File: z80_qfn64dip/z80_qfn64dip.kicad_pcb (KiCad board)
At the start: 4 copper layers, 60 x 23 mm, 48 parts, among them J1 Conn_08, U1 Caravel_QFN, U2 Z80CPU, U3 TPS7A2018PDQNRM3, U4 TPS7A2033PDQNRM3, U5 TPS7A2050PDQNRM3, U6 AT25EU0081A

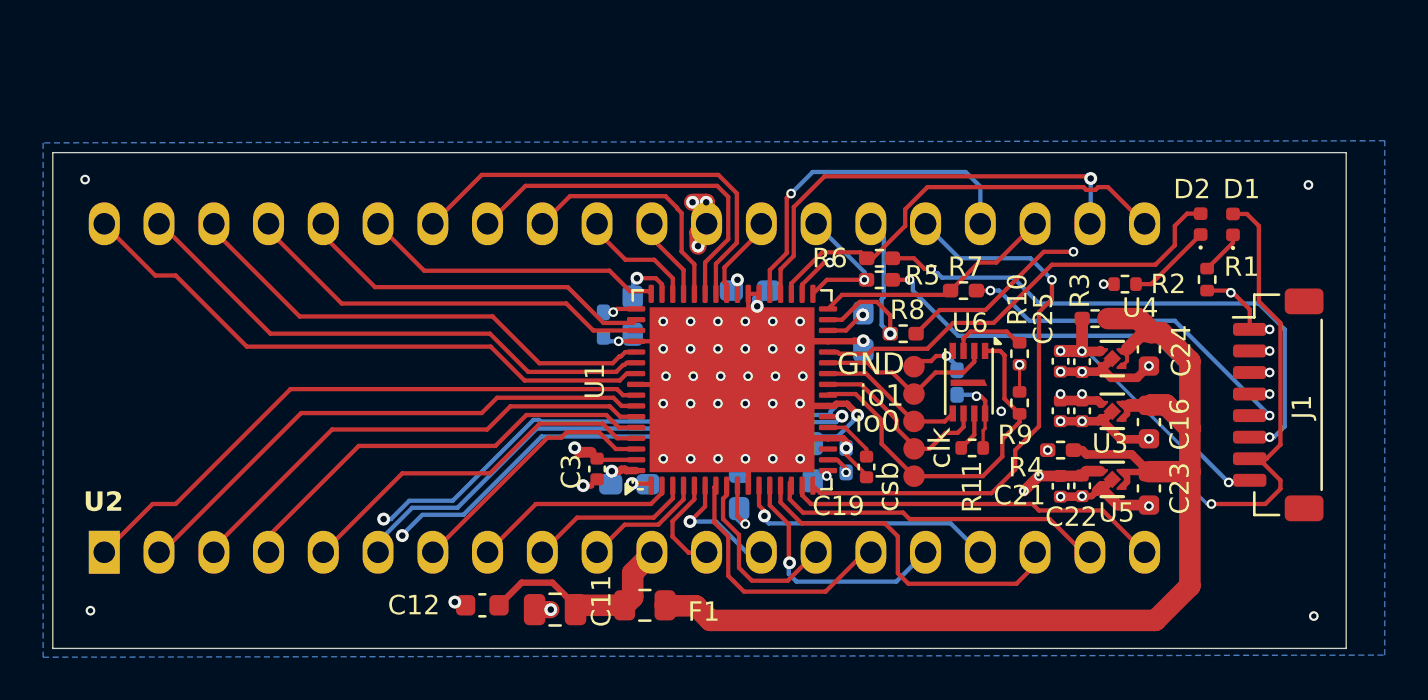
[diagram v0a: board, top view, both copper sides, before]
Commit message: minor layout position tweaks; move schematics around a bit; add aisler user design rule
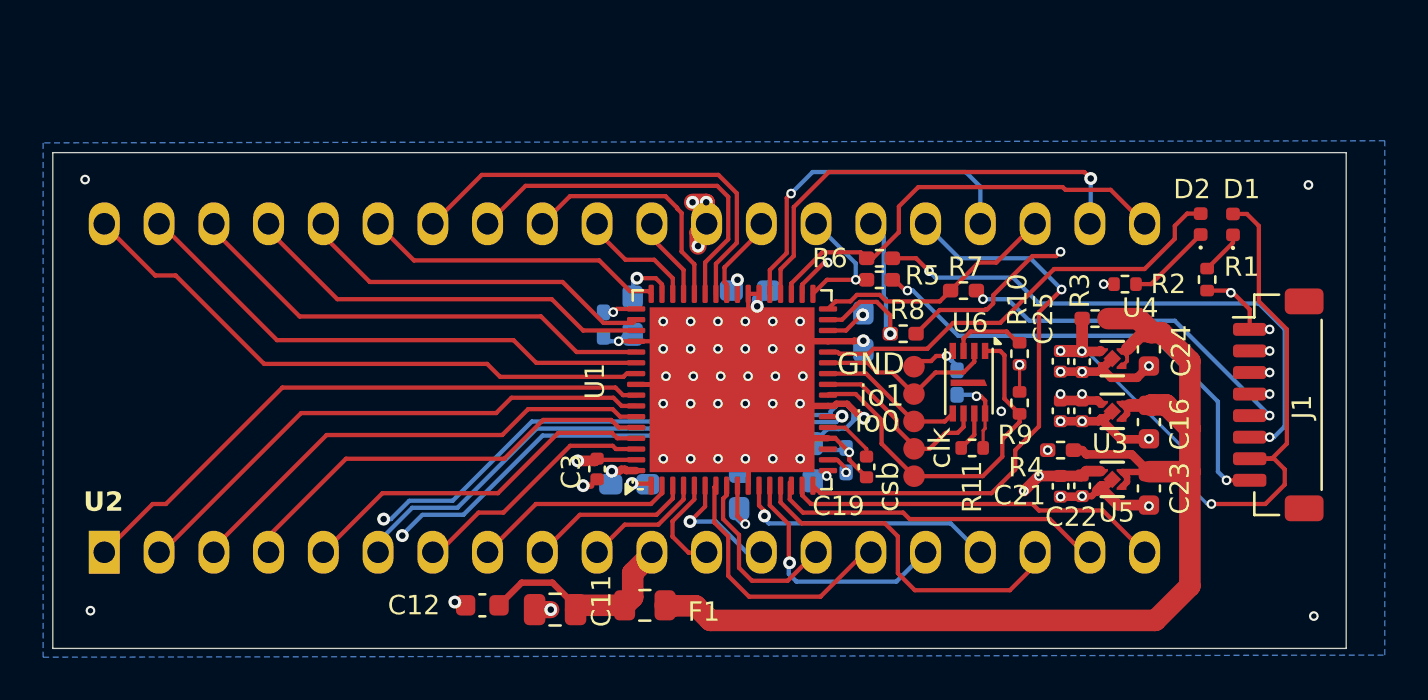
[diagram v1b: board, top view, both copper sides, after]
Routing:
- net GND: track 118.6 -> 121.8 mm
- net HK_CSB: track 26.3 -> 25.2 mm
- net VDDA: track 77.9 -> 78.8 mm
- net /prj_io24: track 12.1 -> 11.6 mm

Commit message: remove signals from power layer moving them to bottom layer; change power routing from tracks to planes if they can be called as such
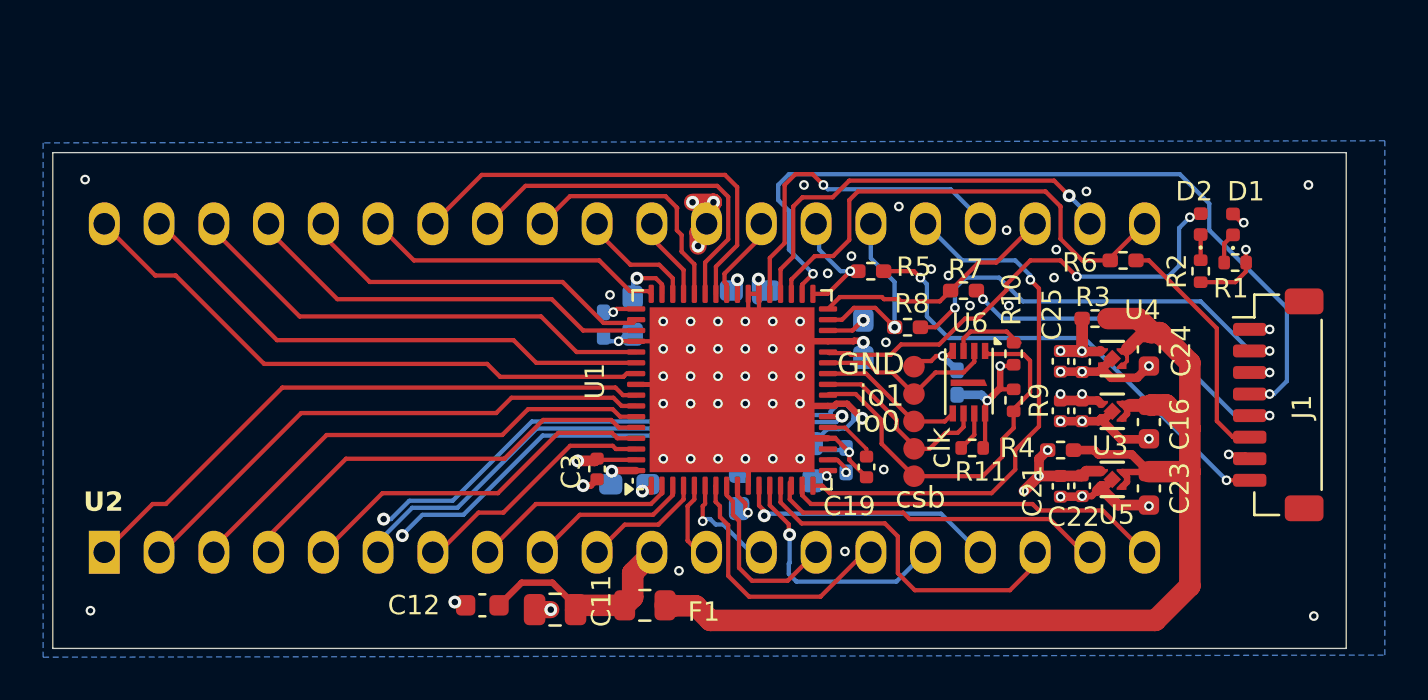
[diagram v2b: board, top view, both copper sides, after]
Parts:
- moved R6 11.3 mm to (166.2, 77.5)
- moved R2 3.56 mm to (169.7, 78.0), turned to -90 degrees
- moved R1 1.52 mm to (171.3, 77.6), turned to 0 degrees
- moved R5 0.57 mm to (154.4, 78.0)
- moved R8 0.36 mm to (156.2, 80.6)
- moved C6 0.34 mm to (154.1, 81.1)
- moved R9 0.30 mm to (161.1, 84.0)
- moved R10 0.28 mm to (161.1, 81.8)
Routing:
- net Net-(J1-Pin_6): track 25.9 -> 11.2 mm, vias 2 -> 0
- net VDDA: track 78.8 -> 66.0 mm, vias 9 -> 10
- net HK_CSB: track 25.2 -> 37.5 mm
- net Net-(D2-K): track 3.95 -> 1.19 mm
- net HK_SCK: track 20.4 -> 22.7 mm
- net VDDIO: track 31.1 -> 29.0 mm
- net /prj_io37: track 26.8 -> 25.5 mm
- net ser_rx: track 21.0 -> 19.6 mm
- net Net-(J1-Pin_2): track 20.1 -> 19.1 mm
- net GND: track 121.8 -> 122.7 mm, vias 63 -> 78
- net flash_csb: track 17.0 -> 18.0 mm
- net gpio: track 20.4 -> 21.3 mm, vias 0 -> 2
- net /prj_io28: track 4.65 -> 3.77 mm
- net HK_JTAG: track 9.82 -> 8.95 mm
- net HK_SDI: track 6.12 -> 5.29 mm
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- added copper zone on In2.Cu, net VCCD
- added copper zone on In2.Cu, net VDDIO

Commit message: minor changes
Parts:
- U3: value TPS7A2018PDQNRM3 -> TPS7A2033PDQNRM3
- U4: value TPS7A2033PDQNRM3 -> TPS7A2018PDQNRM3
- moved U4 2.48 mm to (165.7, 84.5)
- moved U3 2.45 mm to (165.7, 82.1)
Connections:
- U3 pad 1: VCCD -> VDDA
- U4 pad 1: VDDA -> VCCD
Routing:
- net /prj_io10: track 11.4 -> 9.42 mm, vias 0 -> 1
- net GND: vias 78 -> 101
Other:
- board text added: "Z80 V1"

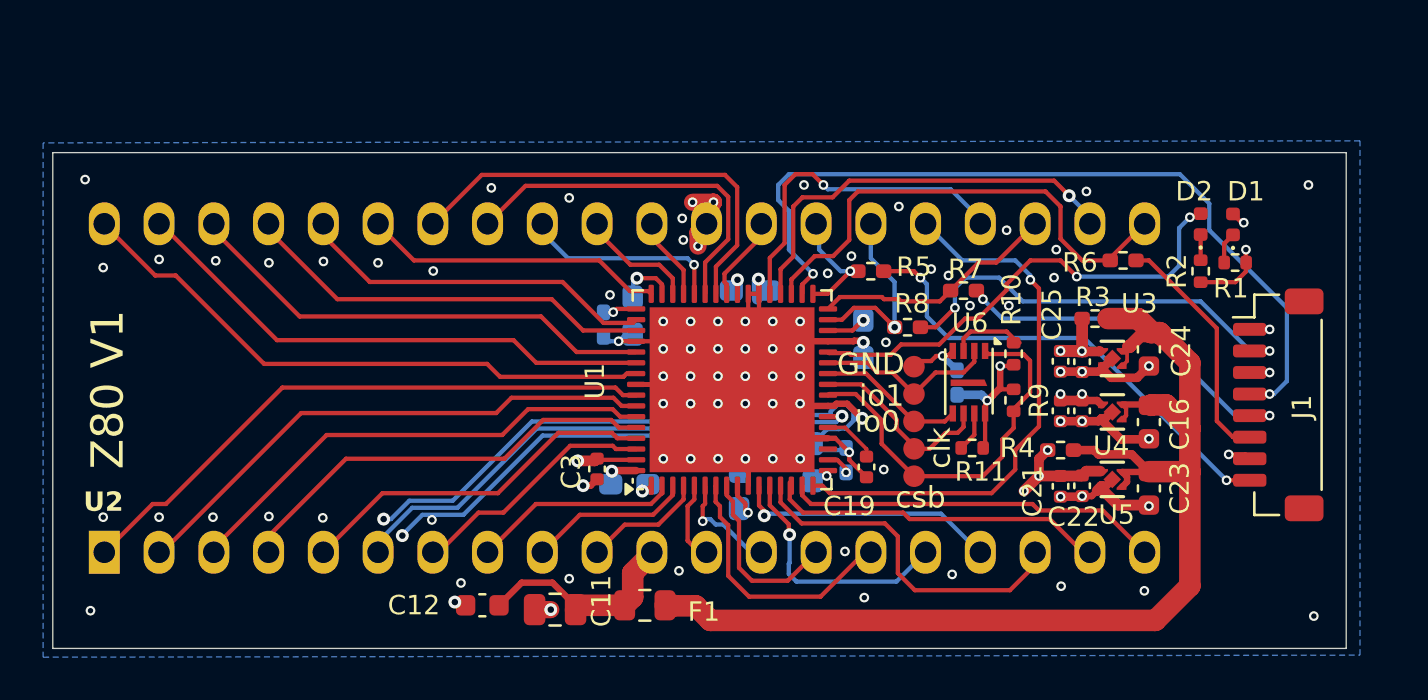
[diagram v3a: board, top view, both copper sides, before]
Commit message: mainly layout changes, remove kicad_prl from comitted files
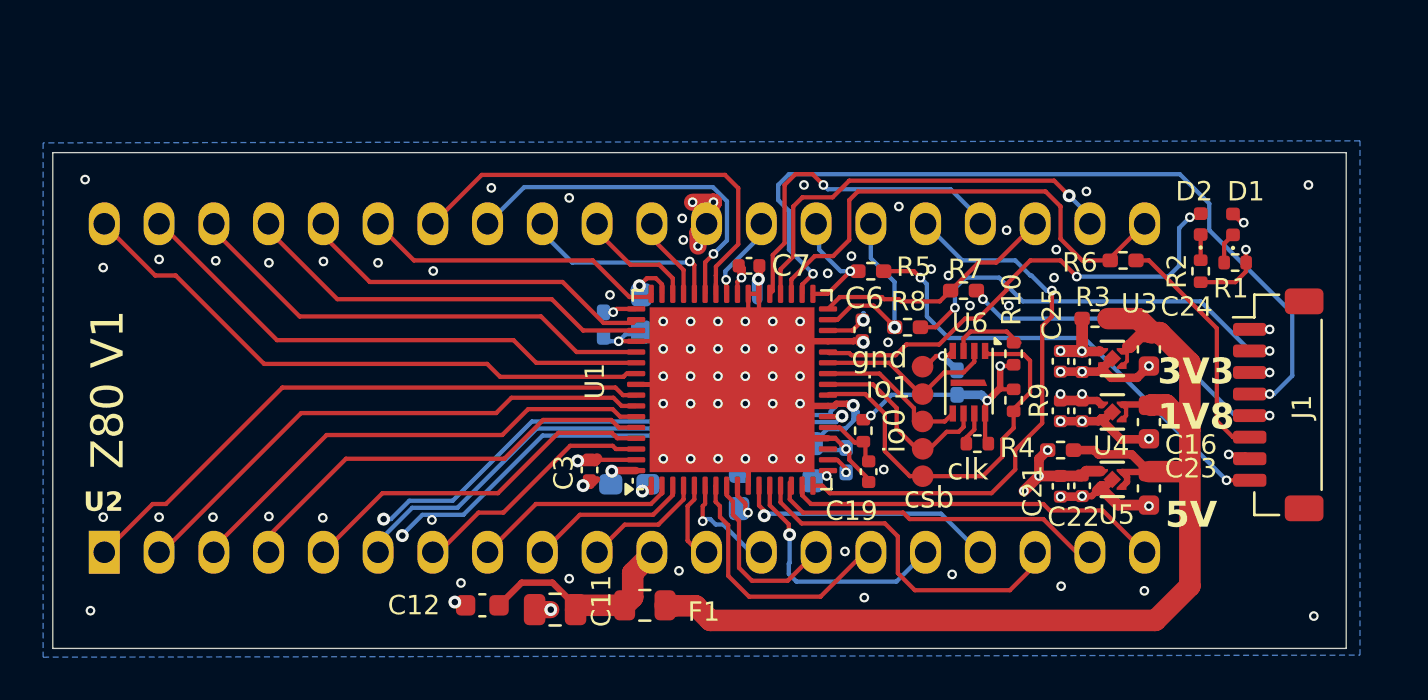
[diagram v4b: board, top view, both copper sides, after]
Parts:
- added R12: 4k7, Resistor_SMD:R_0402_1005Metric, F.Cu at (154.1, 85.4)
- C6, C7: footprint Capacitor_SMD:C_0603_1608Metric_Pad1.08x0.95mm_HandSolder -> Capacitor_SMD:C_0402_1005Metric; moved to F.Cu
- TP13: value GND -> gnd
- moved C7 1.15 mm to (148.8, 77.8)
- moved C6 0.42 mm to (154.0, 80.7)
- moved C8 0.41 mm to (143.8, 80.0)
- moved TP10 0.40 mm to (156.8, 85.0)
- moved TP11 0.40 mm to (156.9, 86.2)
- moved TP12 0.40 mm to (156.9, 87.5)
- moved TP13 0.40 mm to (156.8, 82.4)
- moved TP9 0.40 mm to (156.8, 83.7)
- moved C3 0.35 mm to (141.4, 87.2)
- moved R11 0.31 mm to (159.4, 86.0)
- moved C19 0.24 mm to (154.3, 87.3)
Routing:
- net VDDA: track 66.0 -> 71.4 mm, vias 10 -> 11
- net GND: track 122.7 -> 123.6 mm
- net /prj_io37: track 25.5 -> 26.1 mm
- net gpio: track 21.3 -> 21.9 mm
- net ~{SOC_RST}: track 2.45 -> 2.96 mm
- net /prj_io9: track 17.1 -> 16.8 mm, vias 0 -> 1
- net /prj_io7: vias 0 -> 1
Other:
- board text added: "1V8"
- board text added: "3V3"
- board text added: "5V"

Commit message: move everything to front side; label pins
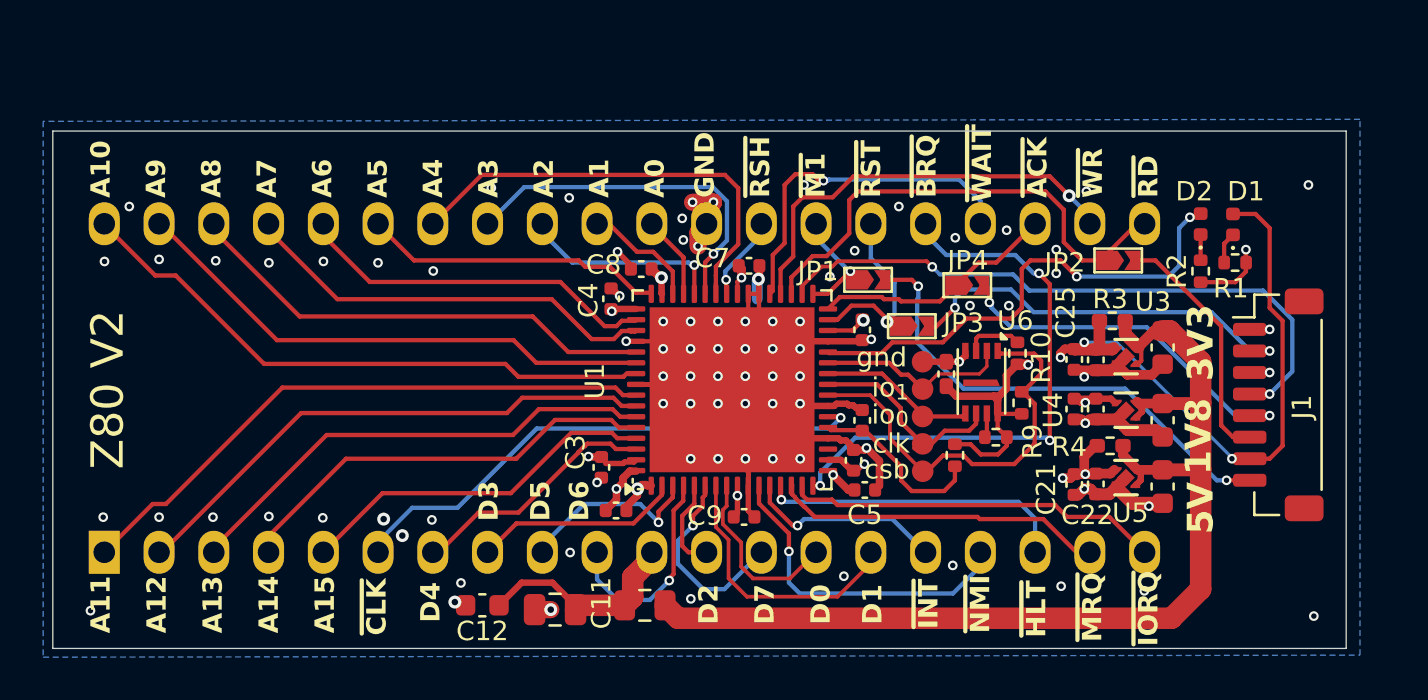
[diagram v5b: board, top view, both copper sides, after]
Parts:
- removed R5, R6, R7, R8: 0R, Resistor_SMD:R_0402_1005Metric_Pad0.72x0.64mm_HandSolder
- added JP1: J_SDI, ProjectLibrary:SolderJumper-2_P2x0.9mm_Open_TrianglePad, F.Cu at (154.3, 78.4)
- added JP2: J_SCK, ProjectLibrary:SolderJumper-2_P2x0.9mm_Open_TrianglePad, F.Cu at (165.9, 77.5)
- added JP3: J_JTAG, ProjectLibrary:SolderJumper-2_P2x0.9mm_Open_TrianglePad, F.Cu at (156.3, 80.6)
- added JP4: J_SDO, ProjectLibrary:SolderJumper-2_P2x0.9mm_Open_TrianglePad, F.Cu at (158.9, 78.7)
- C10, C5, C8, C9: footprint Capacitor_SMD:C_0603_1608Metric_Pad1.08x0.95mm_HandSolder -> Capacitor_SMD:C_0402_1005Metric; moved to F.Cu
- C2, C4: footprint Capacitor_SMD:C_0402_1005Metric_Pad0.74x0.62mm_HandSolder -> Capacitor_SMD:C_0402_1005Metric; moved to F.Cu
- C20: moved to F.Cu
- TP10: value io0 -> io_{0}
- TP9: value io1 -> io_{1}
- moved R12 4.40 mm to (158.3, 86.5)
- moved C5 2.74 mm to (154.2, 88.2), turned to 180 degrees
- moved C19 2.40 mm to (154.0, 84.9), turned to 90 degrees
- moved R4 2.31 mm to (165.5, 86.1)
- moved C8 2.06 mm to (143.8, 77.9), turned to 180 degrees
- moved C10 1.36 mm to (142.6, 89.1)
- moved C9 1.27 mm to (148.6, 89.4), turned to 0 degrees
- moved C4 1.25 mm to (142.4, 79.3), turned to 90 degrees
- moved R11 0.91 mm to (160.2, 85.7)
- moved R3 0.81 mm to (165.7, 80.3)
- moved C16 0.64 mm to (168.0, 84.9)
- moved C17 0.64 mm to (164.9, 84.4)
- moved C18 0.64 mm to (163.9, 84.4)
- moved C21 0.64 mm to (163.9, 87.9)
- moved C22 0.64 mm to (164.9, 87.9)
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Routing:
- net GND: track 123.6 -> 74.5 mm, vias 101 -> 91
- net VCCD: track 41.8 -> 7.83 mm, vias 5 -> 4
- net HK_CSB: track 37.7 -> 29.5 mm
- net ~{SOC_RST}: track 2.96 -> 8.34 mm
- net /prj_io27: track 5.69 -> 10.0 mm, vias 0 -> 1
- net /prj_io29: track 5.10 -> 9.21 mm
- net /VIN_{F}: track 55.0 -> 51.5 mm
- net /prj_io32: track 12.3 -> 15.4 mm
- net /prj_io33: track 11.5 -> 9.22 mm
- net /prj_io34: track 16.3 -> 14.4 mm, vias 0 -> 1
- net VDDIO: track 29.0 -> 30.7 mm, vias 5 -> 4
- net /prj_io26: track 7.25 -> 8.82 mm, vias 0 -> 1
- net VDDA: track 71.4 -> 70.0 mm, vias 11 -> 8
- net Net-(J1-Pin_2): track 19.1 -> 18.1 mm
- net Net-(U6-~{WP}(IO_{2})): track 3.53 -> 2.67 mm
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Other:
- board size 60 x 23 mm -> 60 x 24 mm
- board text added: "A0"
- board text added: "A1"
- board text added: "A10"
- board text added: "A11"
- board text added: "A12"
- board text added: "A13"
- board text added: "A14"
- board text added: "A15"
- board text added: "A2"
- board text added: "A3"
- board text added: "A4"
- board text added: "A5"
- board text added: "A6"
- board text added: "A7"
- board text added: "A8"
- board text added: "A9"
- board text added: "D0"
- board text added: "D1"
- board text added: "D2"
- board text added: "D3"
- board text added: "D4"
- board text added: "D5"
- board text added: "D6"
- board text added: "D7"
- board text added: "GND"
- board text added: "Z80 V2"
- board text added: "~{ACK}"
- board text added: "~{BRQ}"
- board text added: "~{CLK}"
- board text added: "~{HLT}"
- board text added: "~{INT}"
- board text added: "~{IORQ}"
- board text added: "~{M1}"
- board text added: "~{MRQ}"
- board text added: "~{NMI}"
- board text added: "~{RD}"
- board text added: "~{RSH}"
- board text added: "~{RST}"
- board text added: "~{WAIT}"
- board text added: "~{WR}"
- board text removed: "Z80 V1"
